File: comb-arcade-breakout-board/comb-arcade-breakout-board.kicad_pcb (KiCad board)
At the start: 2 copper layers, 114.5 x 13.7 mm, 9 parts, among them J1 Game_Connector, J2 PWR_DANGEROUS, J3 PWR_SAFE, J4 COIN_SLOTS, J5 SPEAKER, J6 VIDEO, J7 MISC_INPUTS, J8 P1, J9 P2

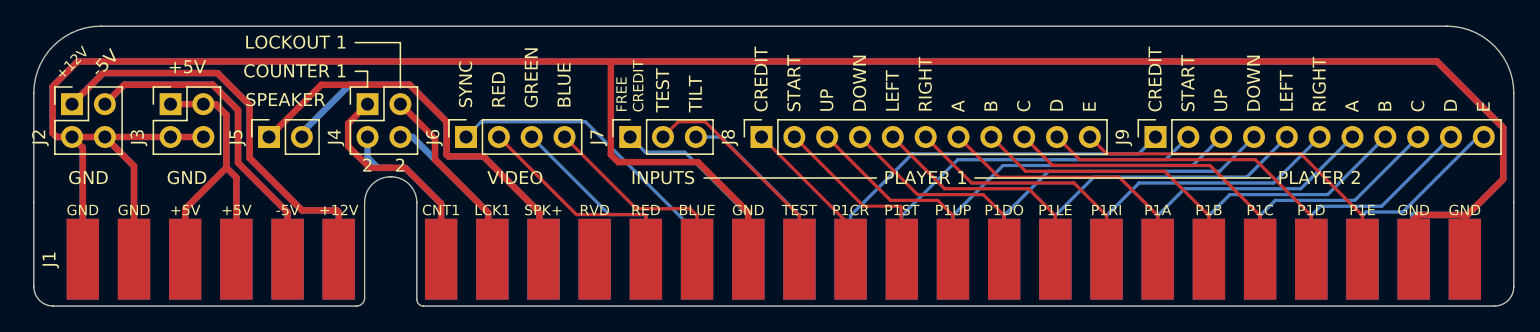
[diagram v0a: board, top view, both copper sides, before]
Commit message: Fix misalignements on comb PCB.
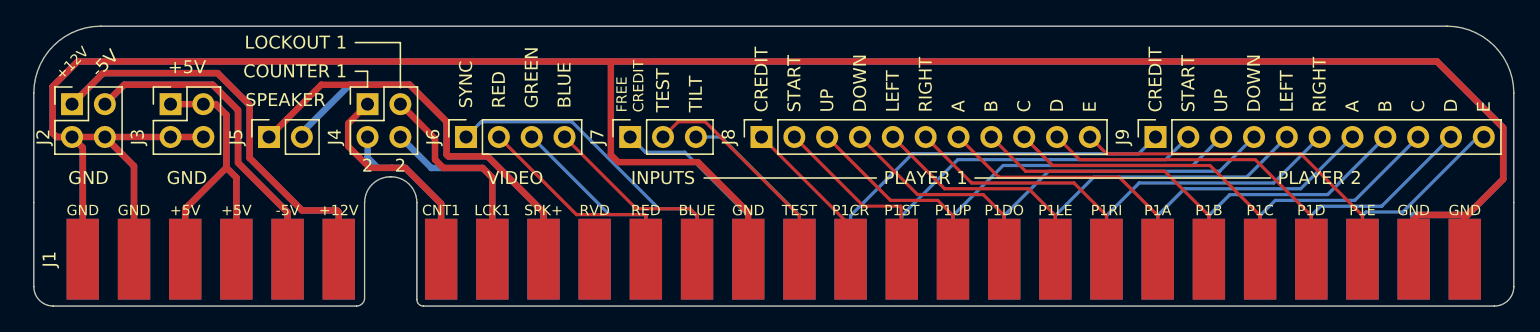
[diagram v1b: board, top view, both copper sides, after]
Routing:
- net LOCKOUT_2: track 12.8 -> 14.7 mm
- net LOCKOUT_1: track 14.8 -> 16.7 mm
- net VIDEO_SYNC: track 23.9 -> 24.7 mm
